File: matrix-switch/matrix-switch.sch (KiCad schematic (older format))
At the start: 0 parts

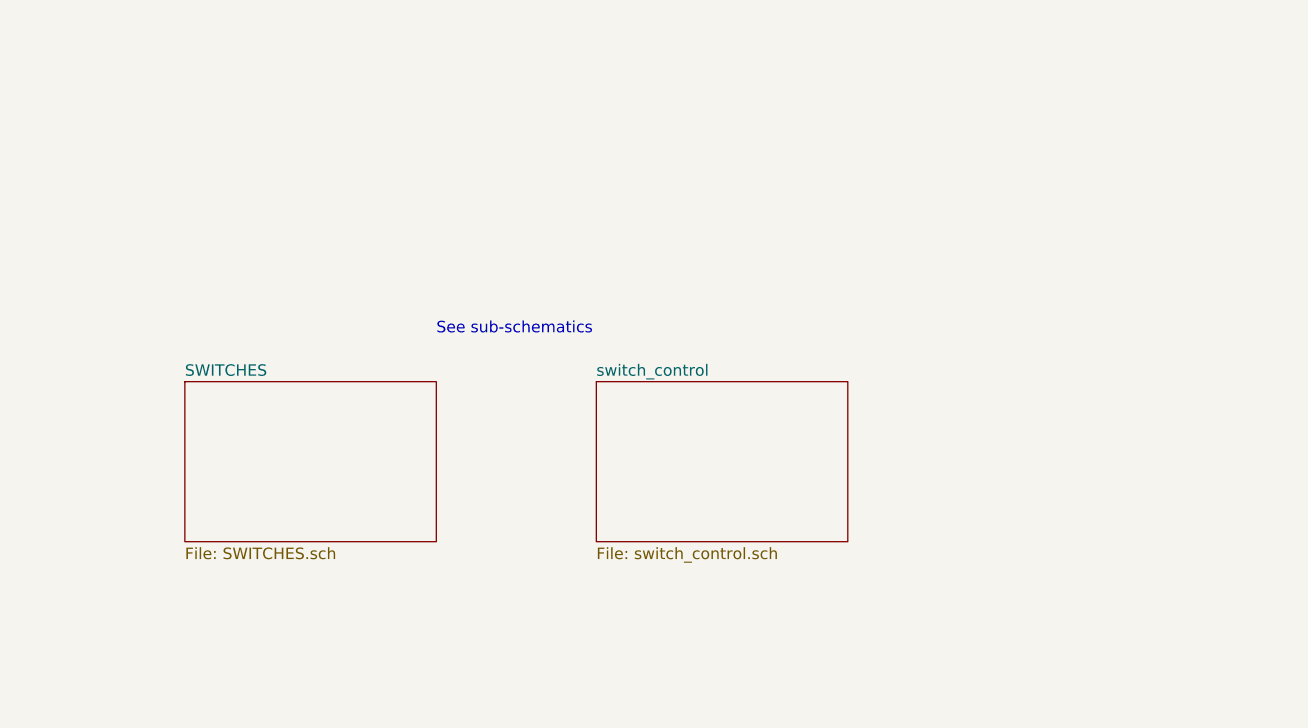
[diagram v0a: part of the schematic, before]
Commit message: wip on matrix switch card edge adapter board
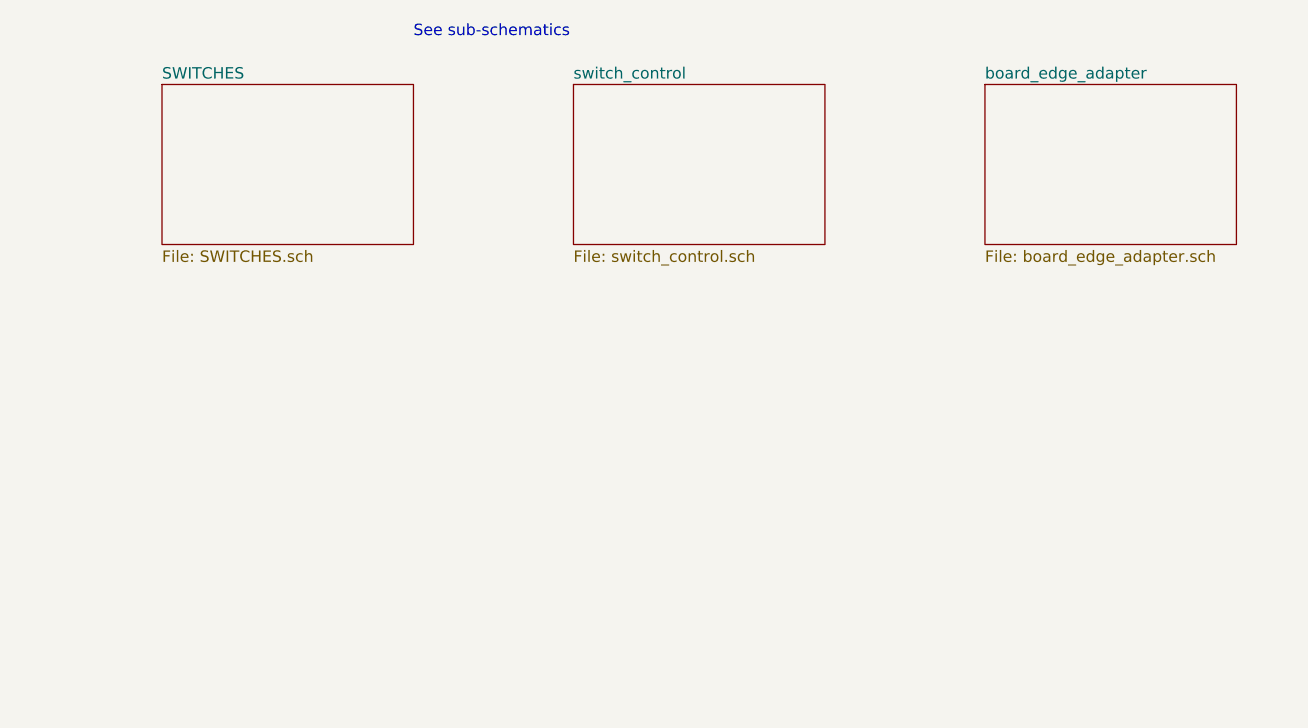
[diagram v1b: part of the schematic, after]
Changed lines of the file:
@@
 $Descr A3 16535 11693
 encoding utf-8
-Sheet 1 3
+Sheet 1 4
 Title ""
 Date ""
@@
 $EndDescr
 $Sheet
-S 6200 5500 1100 700
+S 6100 4200 1100 700
 U 5D997D8A
 F0 "SWITCHES" 50
@@
 $EndComp
 $Sheet
-S 8000 5500 1100 700
+S 7900 4200 1100 700
 U 5D9777B5
 F0 "switch_control" 50
@@
 	1    0    0    -1
 $EndComp
-Text Notes 7300 5300 0    50   ~ 0
+Text Notes 7200 4000 0    50   ~ 0
 See sub-schematics
+$Sheet
+S 9700 4200 1100 700
+U 5D627455
+F0 "board_edge_adapter" 50
+F1 "board_edge_adapter.sch" 50
+$EndSheet
 $EndSCHEMATC
